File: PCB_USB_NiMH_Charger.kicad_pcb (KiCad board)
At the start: 2 copper layers, 94.9 x 72 mm, 45 parts, among them J1 USB_C_Receptacle_Simple, J2 Conn_02x01, J3 Conn_02x01, J4 Conn_02x01, Q1 2SA1015, Q2 2SC1815, Q3 2SB834, Q4 2SC1815, Q5 2SB834, U1 LM393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

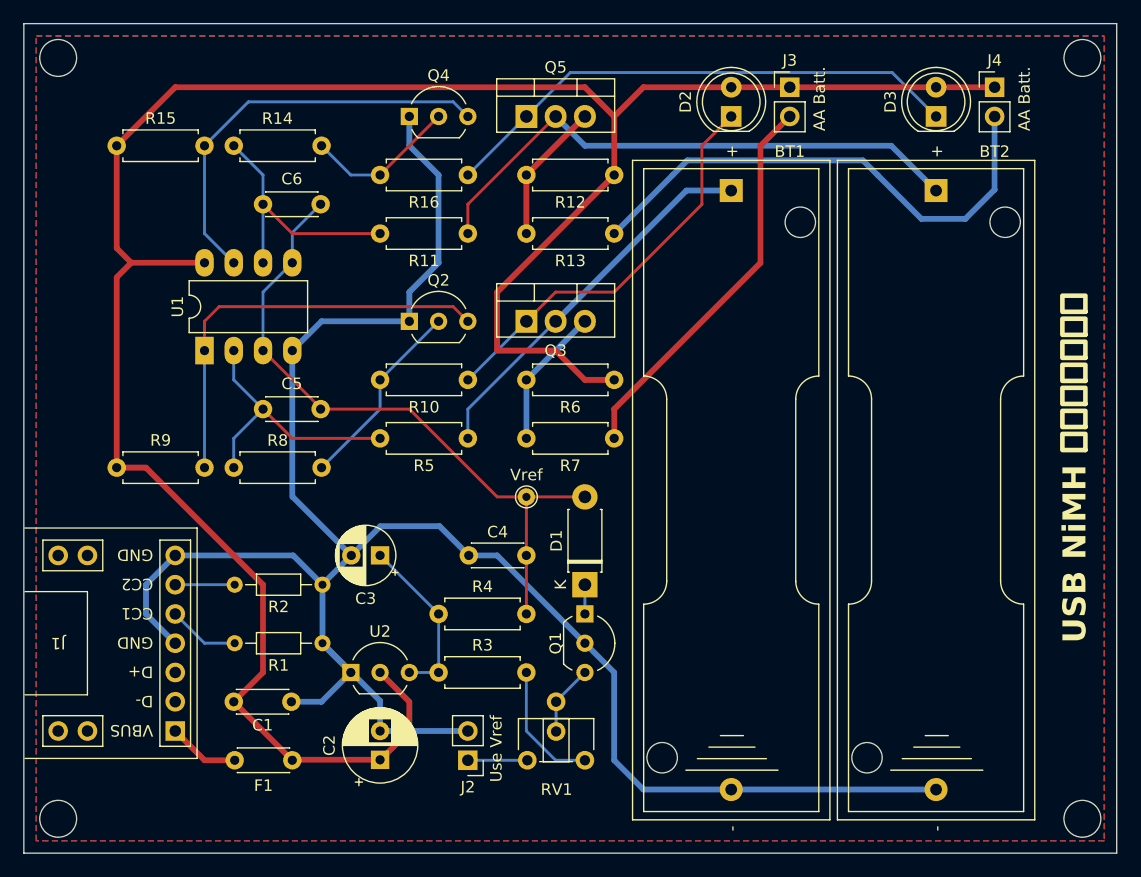
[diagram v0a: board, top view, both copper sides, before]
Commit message: 初版の知見を反映した細かい調整
* VBUSをラベル付け。
* USBコネクタのパッドの穴のサイズを0.9mmに縮小。
* ネットクラスに "Power" を追加。
* D1用にDO-41Sのフットプリントを追加。
* R8, R9, R14, R15 の配置を調整。
* 配線を調整。
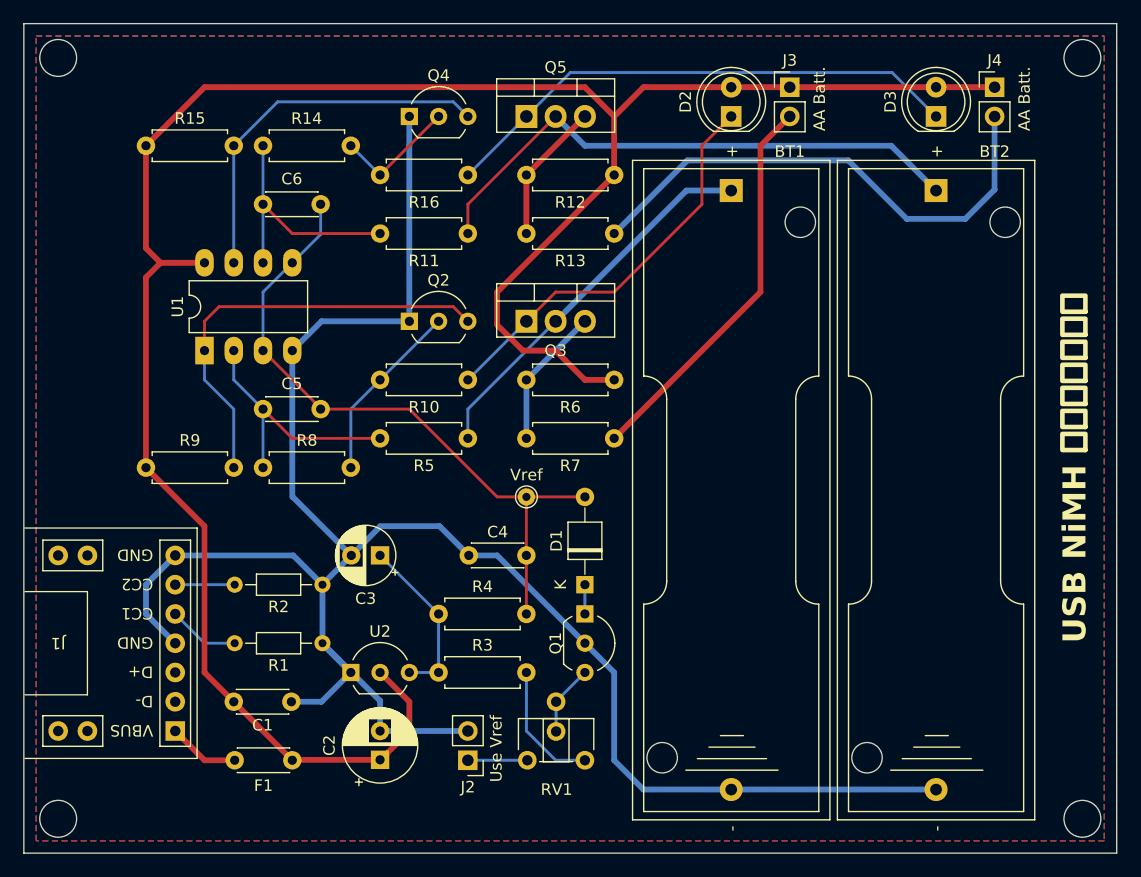
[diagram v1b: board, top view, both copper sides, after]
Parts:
- D1: footprint Diode_THT:D_DO-41_SOD81_P7.62mm_Horizontal -> mylib:D_DO-41S_SOD81_P7.62mm_Horizontal
- moved R14 2.54 mm to (53.3, 66.0)
- moved R8 2.54 mm to (53.3, 94.0)
- moved R15 2.54 mm to (35.6, 66.0)
- moved R9 2.54 mm to (35.6, 94.0)
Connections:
- net Net-(F1-Pad2) renamed /VBUS
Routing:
- net +5V: track 204.1 -> 193.1 mm
- net Net-(Q4-B): track 36.2 -> 32.6 mm
- net Net-(Q4-C): track 13.3 -> 10.8 mm
- net GND: track 176.1 -> 174.0 mm
- net Net-(U1A--): track 23.5 -> 22.4 mm
- net Net-(Q2-C): track 16.9 -> 15.9 mm
- net Net-(U1B--): track 22.4 -> 21.4 mm
- net Net-(Q2-B): track 36.6 -> 37.7 mm

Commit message: パッドとベタの接続形状を調整
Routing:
- net +5V: track 193.1 -> 200.3 mm
- net GND: track 174.0 -> 179.5 mm

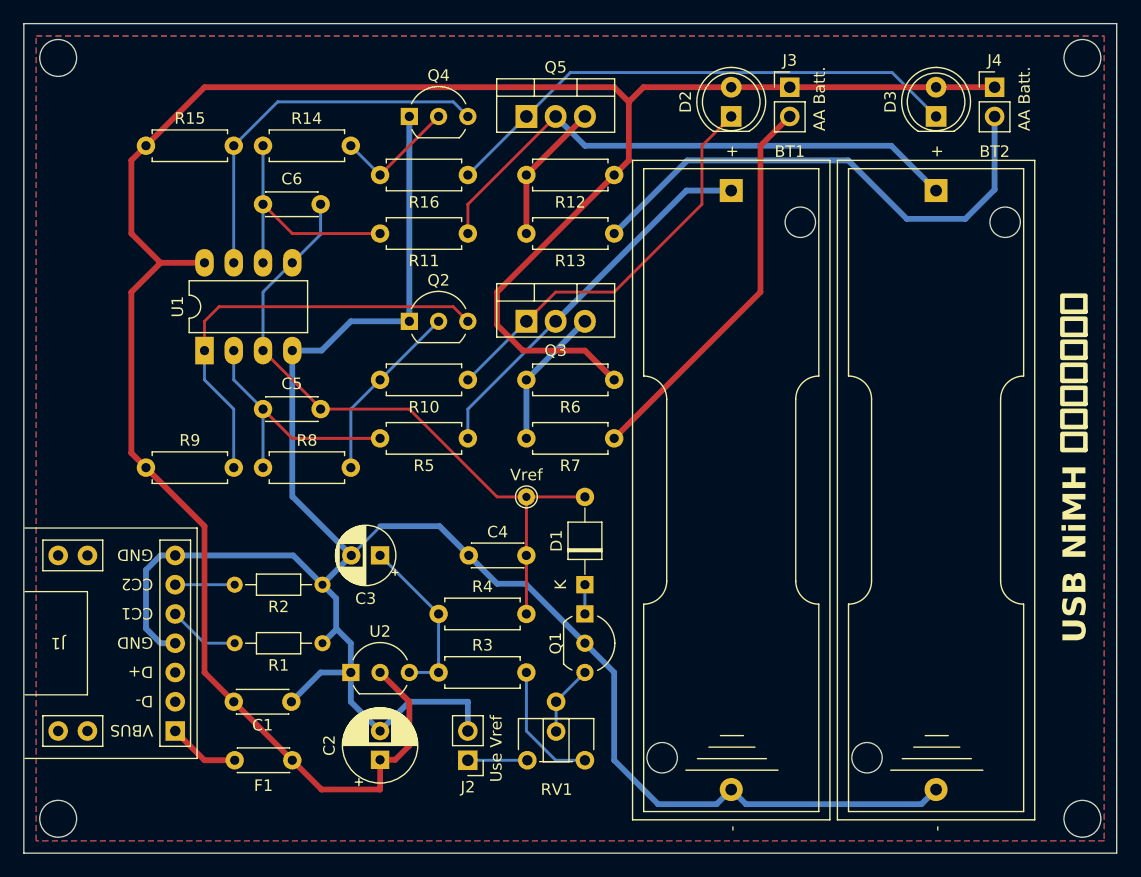
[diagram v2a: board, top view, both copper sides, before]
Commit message: Add rev. 2 silk
* rev. 2 のシルクを追加。
* 配線の表裏を調整。
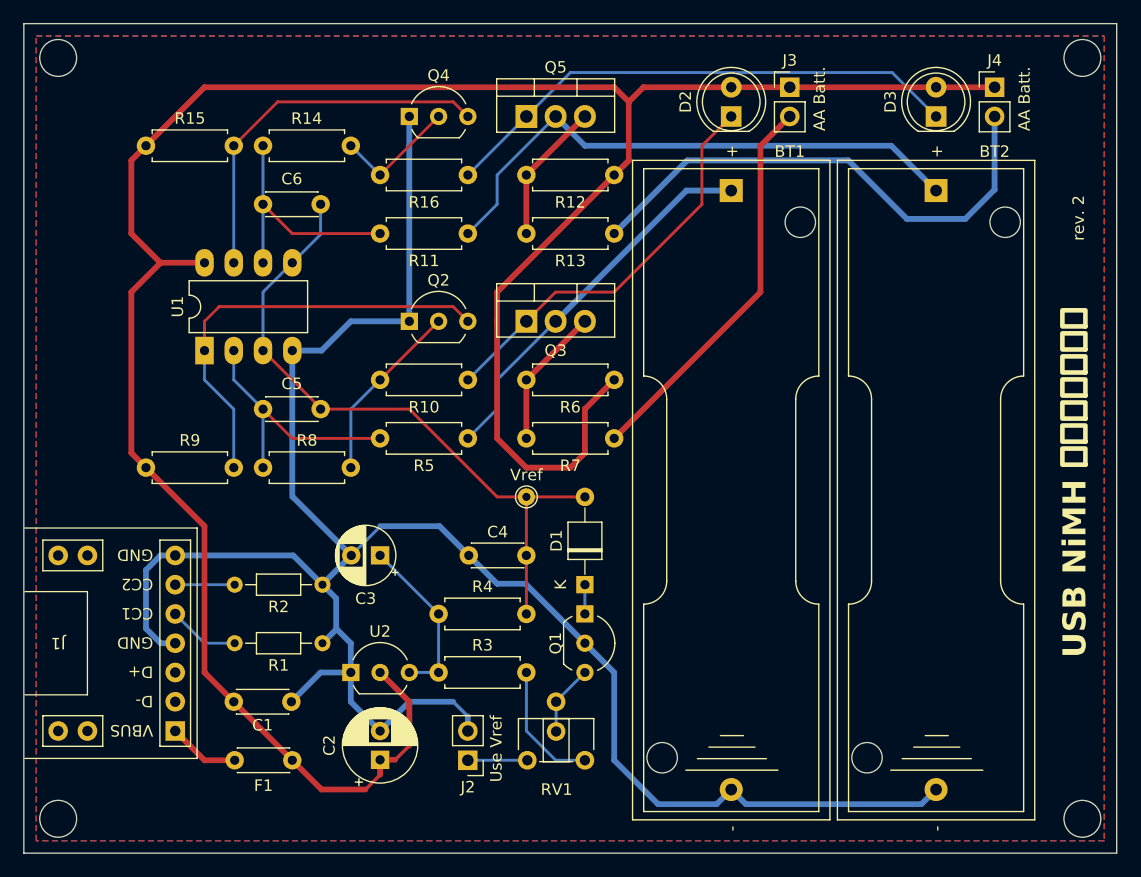
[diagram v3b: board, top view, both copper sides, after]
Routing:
- net +5V: track 200.3 -> 214.2 mm
- net GND: track 179.5 -> 178.7 mm
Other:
- board text added: "rev. 2"

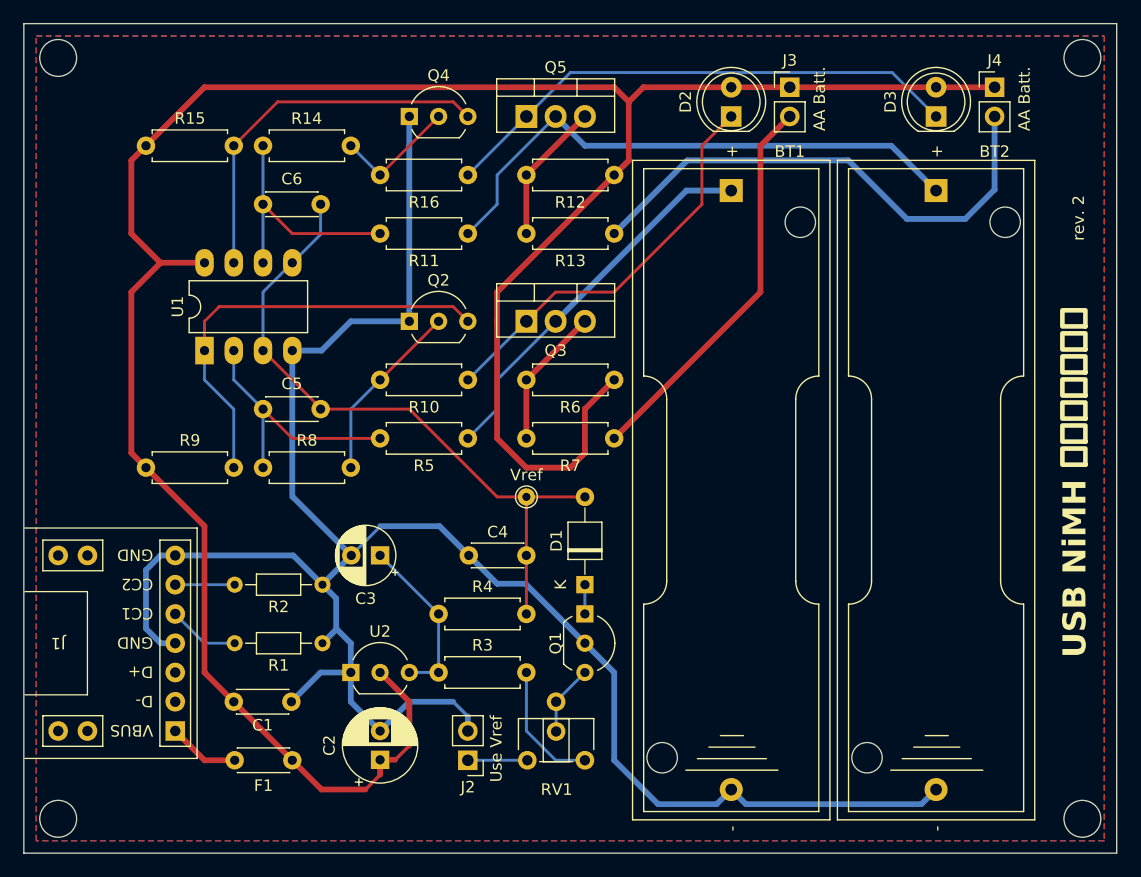
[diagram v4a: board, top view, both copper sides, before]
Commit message: 基板外形を調整
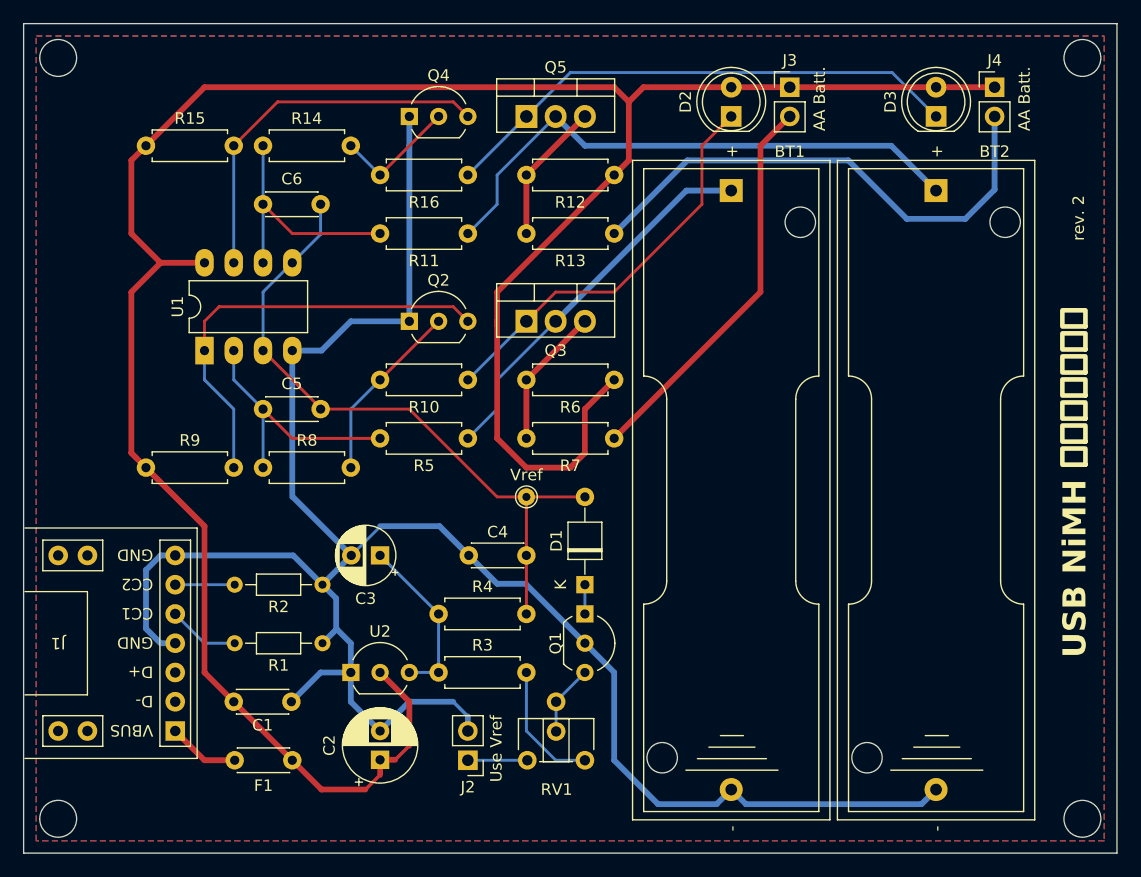
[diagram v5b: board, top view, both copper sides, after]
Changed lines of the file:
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@@
     )
   )
-  (gr_rect (start 24.96 55.44) (end 119.82 127.44)
+  (gr_rect (start 24.94 55.44) (end 119.84 127.44)
     (stroke (width 0.1) (type default)) (fill none) (layer "Edge.Cuts"))
   (gr_text "JLCJLCJLCJLC" (at 116.84 86.36 90) (layer "B.SilkS")
@@
   )
   (dimension (type aligned) (layer "Dwgs.User")
-    (pts (xy 24.96 55.44) (xy 119.82 55.44))
+    (pts (xy 24.94 55.44) (xy 119.84 55.44))
     (height -4.64)
-    (gr_text "94.8600 mm" (at 72.39 49) (layer "Dwgs.User")
+    (gr_text "94.9000 mm" (at 72.39 49) (layer "Dwgs.User")
       (effects (font (size 1.5 1.5) (thickness 0.3)))
     )
